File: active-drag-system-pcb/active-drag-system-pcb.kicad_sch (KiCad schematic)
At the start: 74 parts, among them J1 Conn_01x02_Socket, J1 USB_B_Micro, Q7 DMG1012T, SW1 PTS815 SJM 250 SMTR LFS, U1 TPS51386RJNR, U13 MS5611-01BA, U14 LSM6DSV16XTR, U15 ADXL375BCCZ, U16 IIM-42653, U2 LD39200PU33R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

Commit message: Footprints for IIM; Disconnect AUX1 from GND, Leave as No-Connect
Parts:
- C52: value 10nF -> 10n; footprint (none) -> Capacitor_SMD:C_0201_0603Metric_Pad0.64x0.40mm_HandSolder; Dielectric (none) -> X7R; Max Voltage (none) -> 6.3V; Tolerance (none) -> 10%
- C53: value 100nF -> 100n; footprint (none) -> Capacitor_SMD:C_0201_0603Metric_Pad0.64x0.40mm_HandSolder; Dielectric (none) -> X7R; Max Voltage (none) -> 6.3V; Tolerance (none) -> 10%
- C54: value 2200nF -> 2.2u; footprint (none) -> Capacitor_SMD:C_0402_1005Metric_Pad0.74x0.62mm_HandSolder; Dielectric (none) -> X7R; Max Voltage (none) -> 6.3V; Tolerance (none) -> 10%
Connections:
- net GPIO20 is gone; now on net I2C0_SDA: U5.31 (GPIO20)
- net GPIO23 is gone; now on net RP2040_CLKOUT1: U5.35 (GPIO23)
- net -BATT: no longer U16.10 (AUX1_CS), U16.11 (AUX1_SDO), U16.2 (AUX1_SDIO), U16.3 (AUX1_SCLK)
- net I2C0_SCL: now also U5.32 (GPIO21); no longer U5.3 (GPIO1)
- net I2C0_SDA: no longer U5.2 (GPIO0)
- net GPIO11 renamed NLIN_C
- net GPIO13 renamed HALL_A
- net GPIO14 renamed HALL_B
- net GPIO15 renamed HALL_C
- net GPIO18 renamed I2C1_SDA
- net GPIO19 renamed I2C1_SCL
- net GPIO21 renamed RP2040_CLKOUT1
- net RP2040_CLKOUT1: no longer U5.32 (GPIO21)
- net GPIO3 renamed HIN_B
- net GPIO5 renamed HIN_C
- net GPIO7 renamed NLIN_A
- net GPIO9 renamed NLIN_B
- new net GPIO0: U5.2 (GPIO0)
- new net HIN_A: U5.3 (GPIO1)
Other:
- note added: "Mid-G IMU"
- note removed: "This one's crazy"
- moved on the sheet: C13, C14, C15, C16, C17, C18, C19, C20, C21, C22, C23, C24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

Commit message: resizing schematic
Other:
- note added: "Motor Control"
- note added: "RP2040 (Primary MCU)"
- note added: "Sensors"
- moved on the sheet: C1, C10, C11, C12, C13, C14, C15, C16, C17, C18, C19, C2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

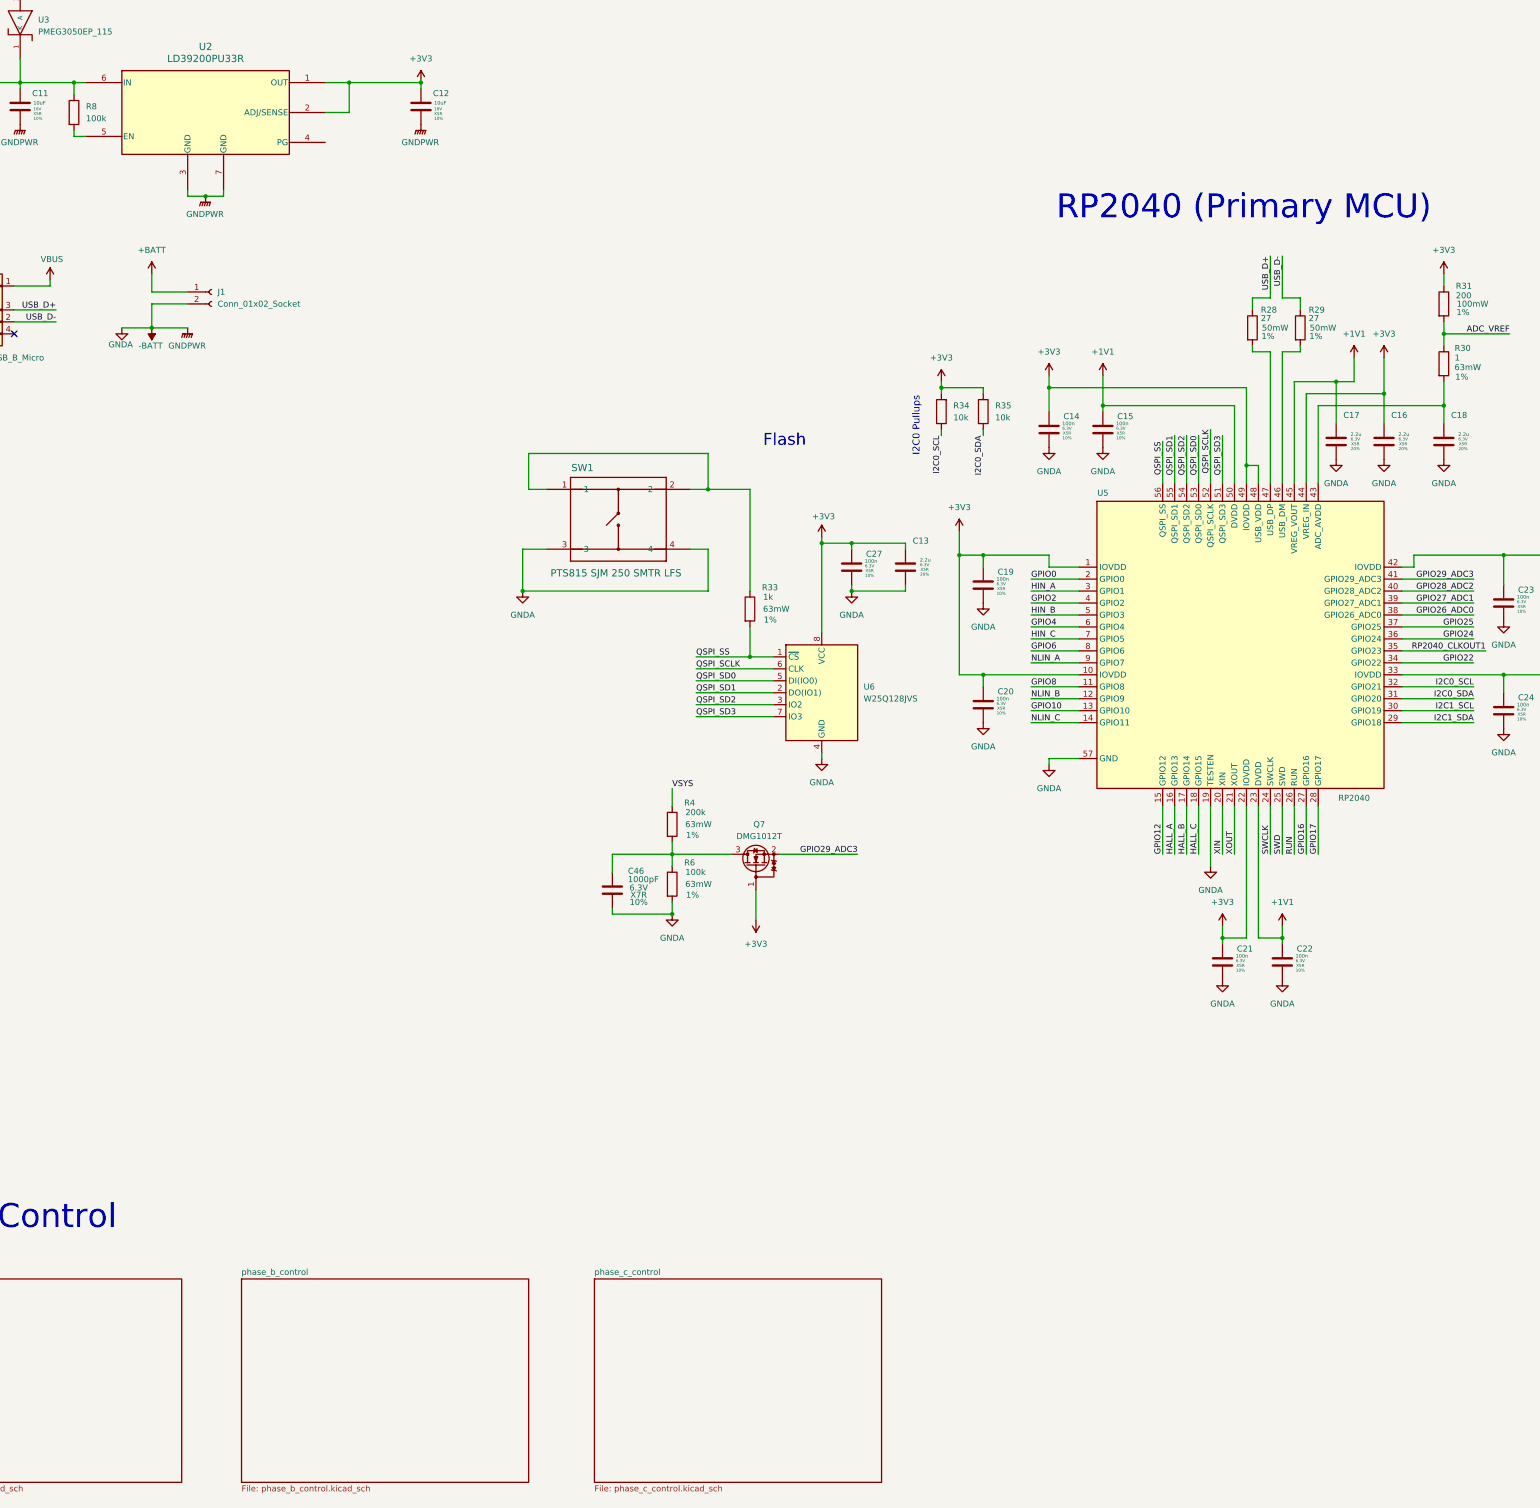
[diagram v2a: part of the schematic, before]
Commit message: Updated Footprint library; Started component placement for 5V regulator
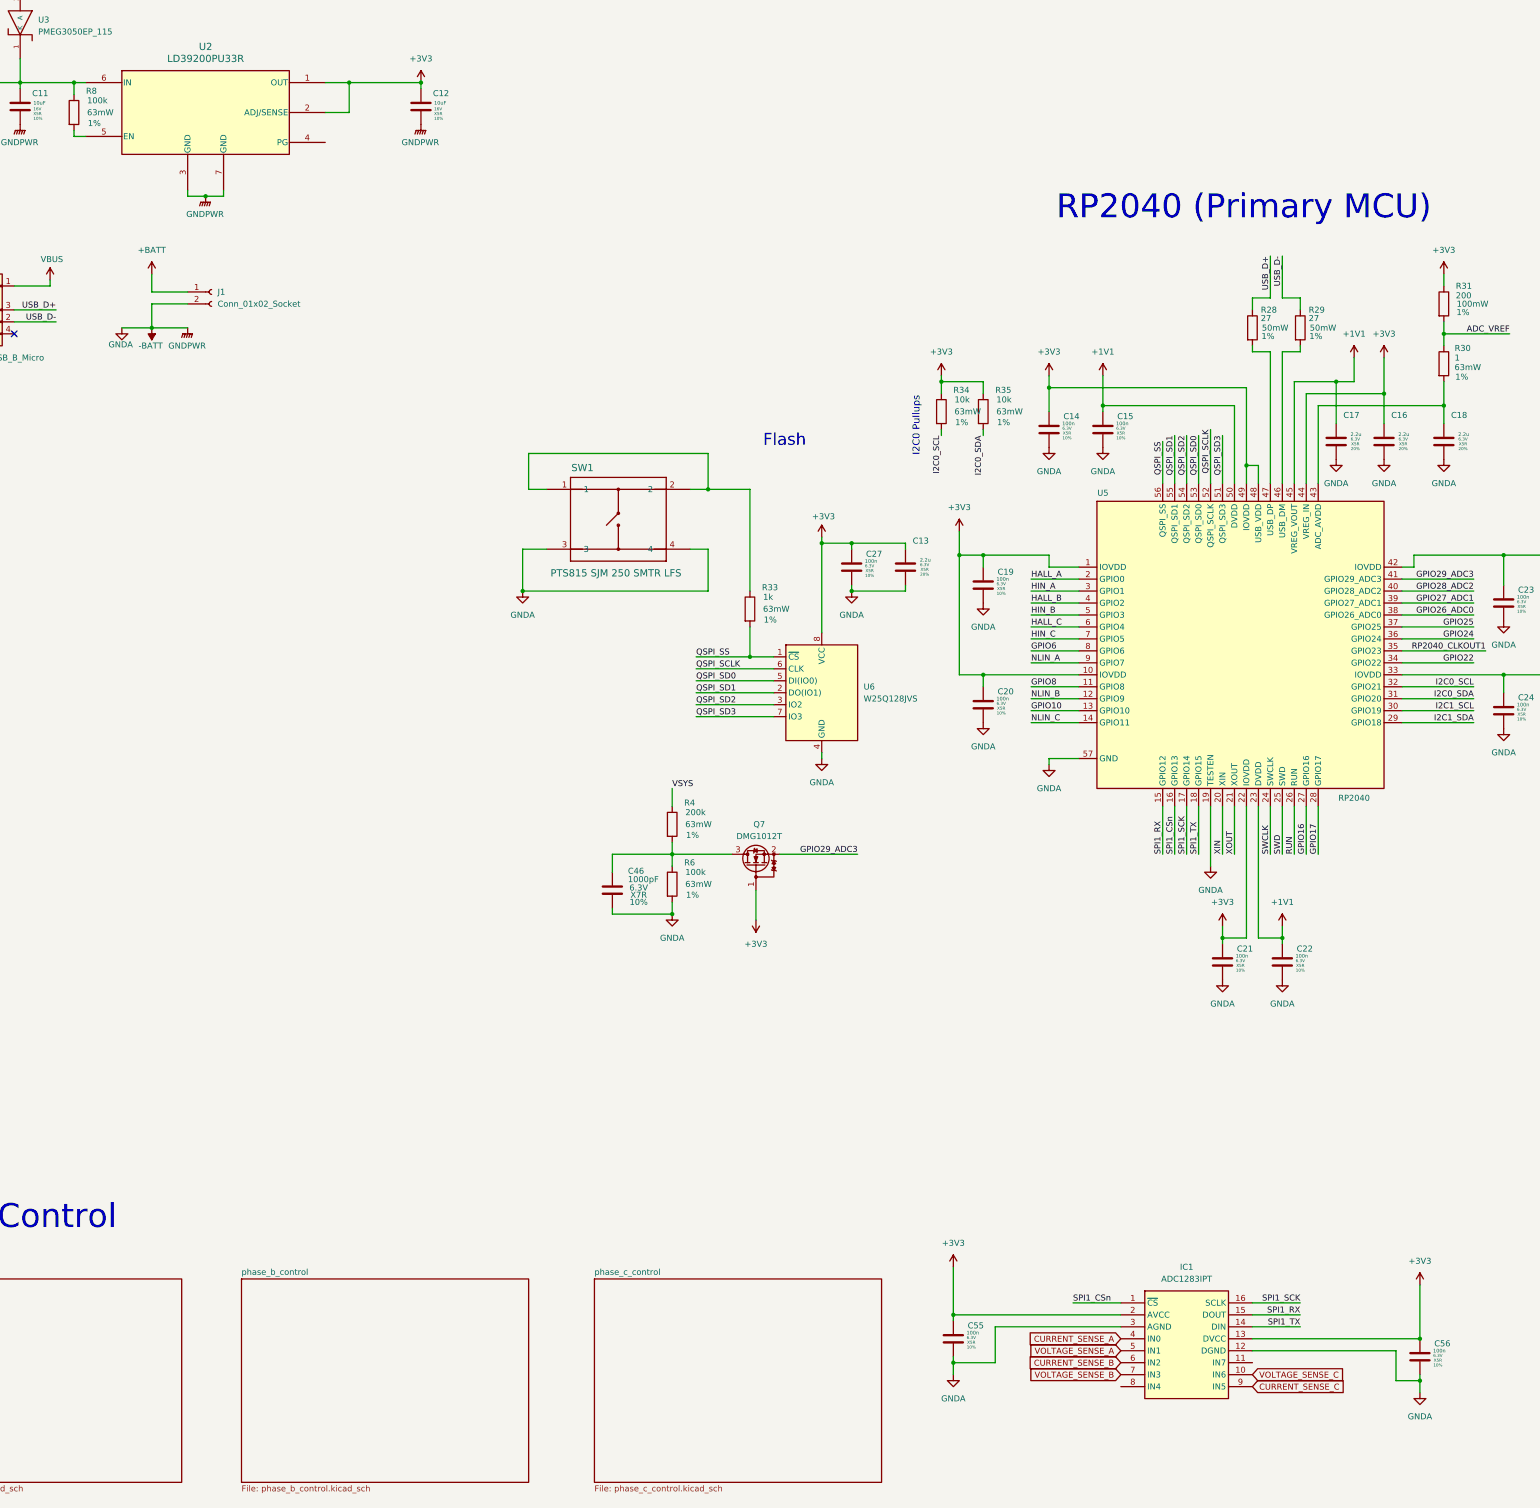
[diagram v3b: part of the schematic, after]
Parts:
- added C55, C56: 100n, Capacitor_SMD:C_0201_0603Metric_Pad0.64x0.40mm_HandSolder, symbol Device:C
- added IC1: ADC1283IPT, ADS_Library:SOP65P640X120-16N, symbol ADC1283IPT:ADC1283IPT
- D7: footprint WL-SMCW_0603:WL-SMCW_0603 -> ADS_Library:WL-SMCW_0603
- J1: footprint RP2040_minimal:USB_Micro-B_Amphenol_10103594-0001LF_Horizontal_modified -> Connector_USB:USB_Micro-B_Amphenol_10103594-0001LF_Horizontal
- R34: footprint Resistor_SMD:R_0201_0603Metric_Pad0.64x0.40mm_HandSolder -> Resistor_SMD:R_0402_1005Metric_Pad0.72x0.64mm_HandSolder; Power (none) -> 63mW; Tolerance (none) -> 1%
- R35, R8: footprint (none) -> Resistor_SMD:R_0402_1005Metric_Pad0.72x0.64mm_HandSolder; Power (none) -> 63mW; Tolerance (none) -> 1%
- U1: footprint TPS51386RJNR:VREG_TPS51386RJNR -> ADS_Library:VREG_TPS51386RJNR
- U16: footprint IIM-42653:PQFN50P250X300X97-14N -> PQFN50P250X300X97-14N
- U3, U4: footprint PMEG3050EP_115:SODFL4725X110N -> ADS_Library:SODFL4725X110N
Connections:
- net GPIO0 is gone; now on net HALL_A: U5.2 (GPIO0)
- net GPIO2 is gone; now on net HALL_B: U5.4 (GPIO2)
- net GPIO4 is gone; now on net HALL_C: U5.6 (GPIO4)
- net +3V3: now also R34.1, C55.1, C56.1, IC1.13 (DVCC), IC1.2 (AVCC); no longer R34.2
- net -BATT: now also C55.2, C56.2, IC1.12 (DGND), IC1.3 (AGND)
- net HALL_A: no longer U5.16 (GPIO13)
- net HALL_B: no longer U5.17 (GPIO14)
- net HALL_C: no longer U5.18 (GPIO15)
- net I2C0_SCL: now also R34.2; no longer R34.1
- net GPIO12 renamed SPI1_RX
- net SPI1_RX: now also IC1.15 (DOUT)
- new net CURRENT_SENSE_A: IC1.4 (IN0)
- new net CURRENT_SENSE_B: IC1.6 (IN2)
- new net CURRENT_SENSE_C: IC1.9 (IN5)
- new net SPI1_CSn: IC1.1 (~{CS}), U5.16 (GPIO13)
- new net SPI1_SCK: IC1.16 (SCLK), U5.17 (GPIO14)
- new net SPI1_TX: IC1.14 (DIN), U5.18 (GPIO15)
- new net VOLTAGE_SENSE_A: IC1.5 (IN1)
- new net VOLTAGE_SENSE_B: IC1.7 (IN3)
- new net VOLTAGE_SENSE_C: IC1.10 (IN6)
